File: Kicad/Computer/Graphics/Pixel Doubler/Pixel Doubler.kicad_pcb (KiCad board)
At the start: 2 copper layers, 26.7 x 49.5 mm, 17 parts, among them IC1 PI3B3251QE, IC2 74LVC16373ADL,118, IC3 74LVC2G08DP-Q100H, IC4 74LVC2G04GW-Q100H, IC5 PI3B3251QE, IC6 74LVC163PW,118, IC7 AP7365-33WG-7, J1 Conn_02x16_Counter_Clockwise

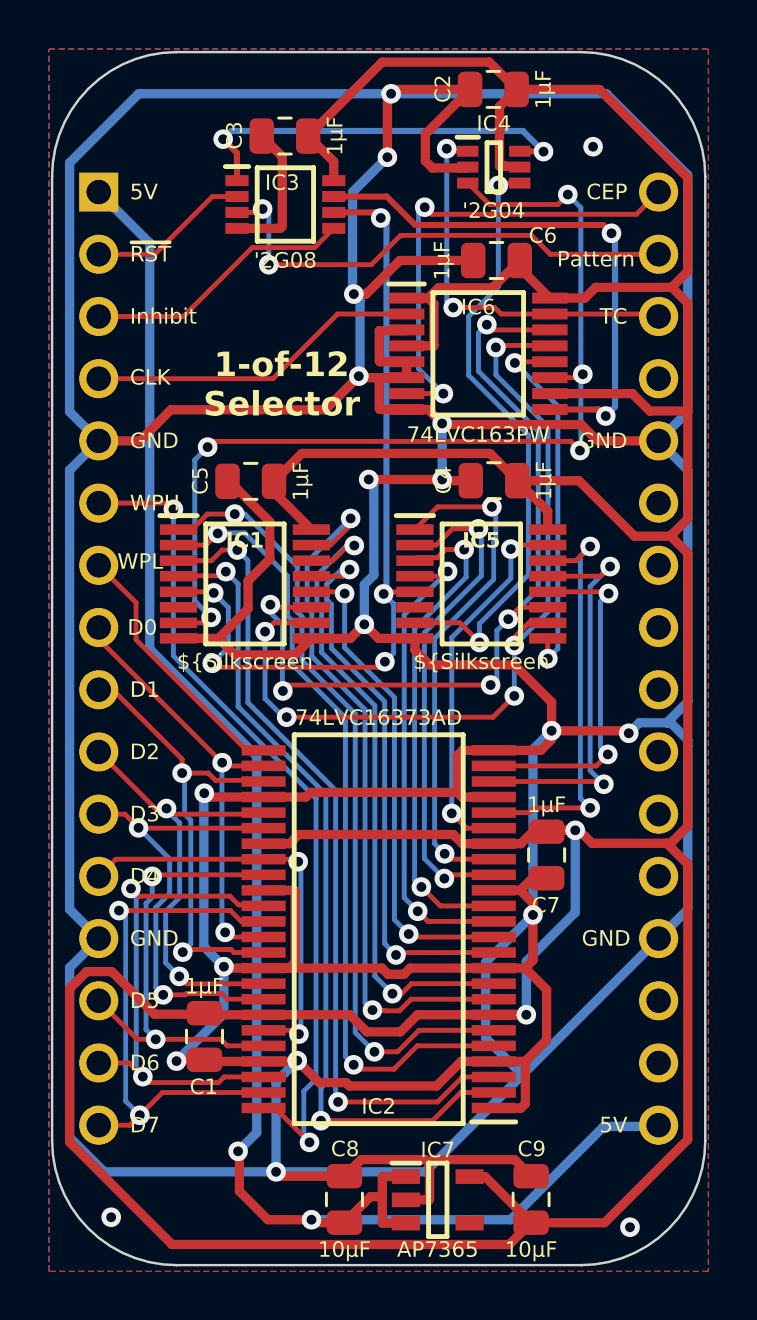
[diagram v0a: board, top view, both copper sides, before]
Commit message: Standardising DIP board layouts.
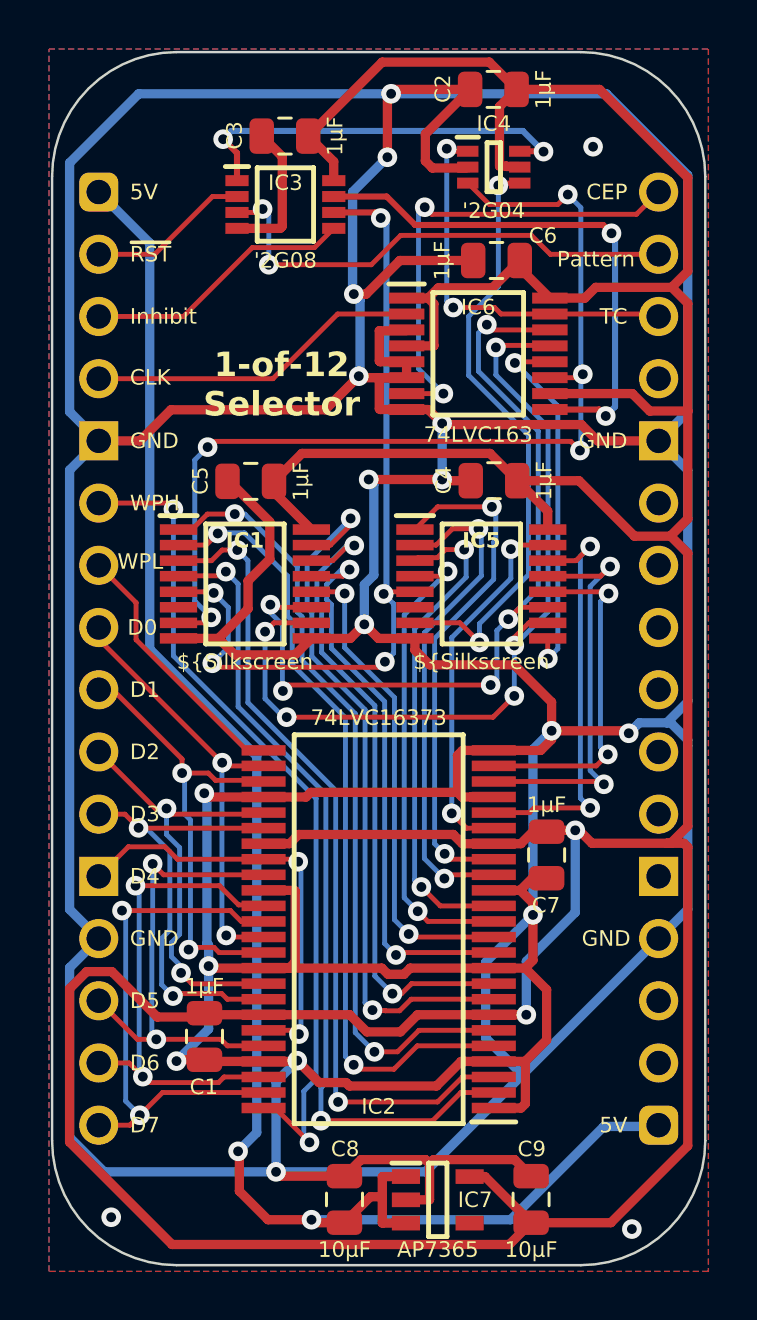
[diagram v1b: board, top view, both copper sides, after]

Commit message: Fixed and labeled the Pixel Pixel Doubler (1-of-12 selector).
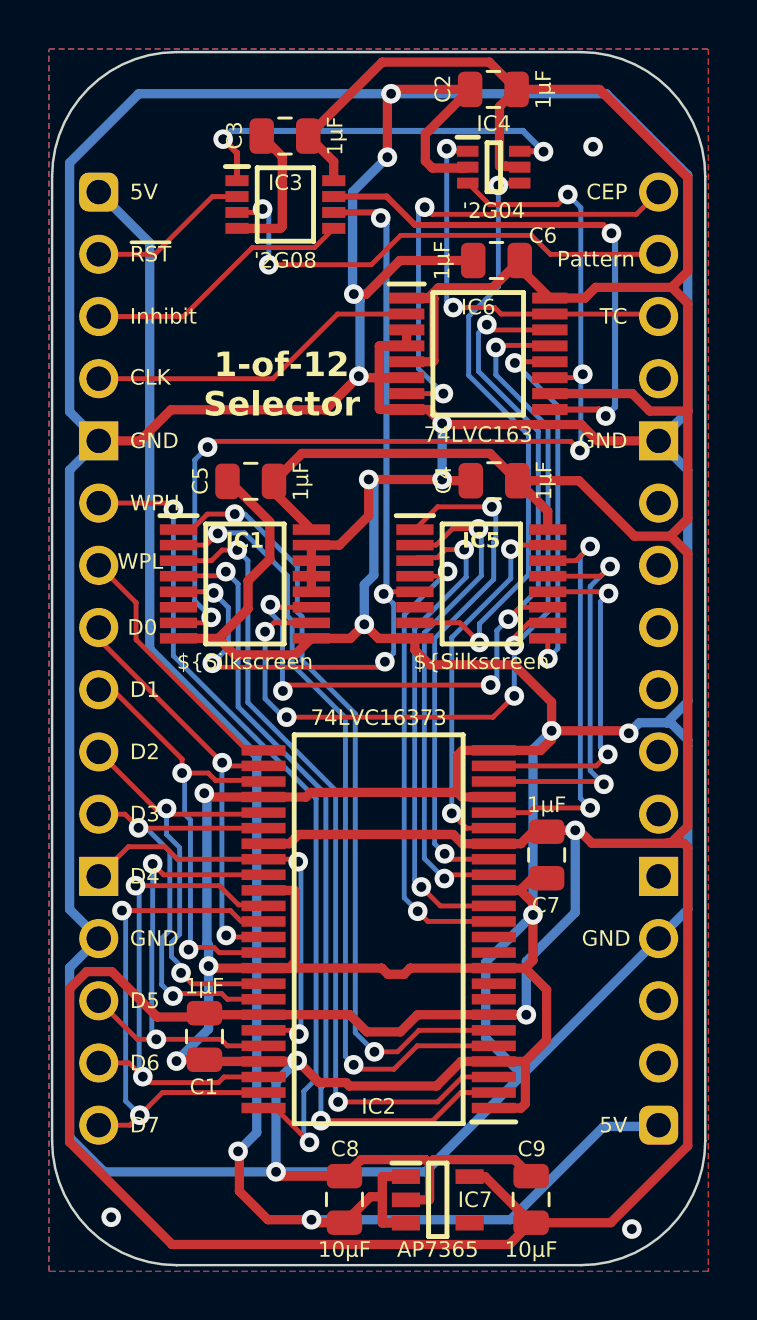
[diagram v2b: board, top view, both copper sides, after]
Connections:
- IC1 pad 1: /RPS11 -> /RPS8
- IC1 pad 12: /RPS15 -> /GND
- IC1 pad 13: /RPS14 -> /GND
- IC1 pad 14: /RPS13 -> /GND
- IC1 pad 15: /RPS12 -> /GND
- IC1 pad 2: /RPS10 -> /RPS9
- IC1 pad 3: /RPS9 -> /RPS10
- IC1 pad 4: /RPS8 -> /RPS11
- IC2 pad 11: /RPS14 -> unconnected-(IC2-1Q6-Pad11)
- IC2 pad 12: /RPS15 -> unconnected-(IC2-1Q7-Pad12)
- IC2 pad 13: /RPS0 -> /RPS7
- IC2 pad 14: /RPS1 -> /RPS6
- IC2 pad 16: /RPS2 -> /RPS5
- IC2 pad 17: /RPS3 -> /RPS4
- IC2 pad 19: /RPS4 -> /RPS3
- IC2 pad 2: /RPS8 -> /RPS11
- IC2 pad 20: /RPS5 -> /RPS2
- IC2 pad 22: /RPS6 -> /RPS1
- IC2 pad 23: /RPS7 -> /RPS0
- IC2 pad 25: /Write Pattern Low -> /Write Pattern High
- IC2 pad 26: /D0 -> /D7
- IC2 pad 27: /D1 -> /D6
- IC2 pad 29: /D2 -> /D5
- IC2 pad 3: /RPS9 -> /RPS10
- IC2 pad 30: /D3 -> /D4
- IC2 pad 32: /D4 -> /D3
- IC2 pad 33: /D5 -> /D2
- IC2 pad 35: /D6 -> /D1
- IC2 pad 36: /D7 -> /D0
- IC2 pad 37: /D0 -> /D7
- IC2 pad 38: /D1 -> /D6
- IC2 pad 40: /D2 -> /D5
- IC2 pad 41: /D3 -> /D4
- IC2 pad 43: /D4 -> /D3
- IC2 pad 44: /D5 -> /D2
- IC2 pad 46: /D6 -> /D1
- IC2 pad 47: /D7 -> /D0
- IC2 pad 48: /Write Pattern High -> /Write Pattern Low
- IC2 pad 5: /RPS10 -> /RPS9
- IC2 pad 6: /RPS11 -> /RPS8
- IC2 pad 8: /RPS12 -> unconnected-(IC2-1Q4-Pad8)
- IC2 pad 9: /RPS13 -> unconnected-(IC2-1Q5-Pad9)
- IC5 pad 1: /RPS3 -> /RPS4
- IC5 pad 12: /RPS7 -> /RPS0
- IC5 pad 13: /RPS6 -> /RPS1
- IC5 pad 14: /RPS5 -> /RPS2
- IC5 pad 15: /RPS4 -> /RPS3
- IC5 pad 2: /RPS2 -> /RPS5
- IC5 pad 3: /RPS1 -> /RPS6
- IC5 pad 4: /RPS0 -> /RPS7
- IC6 pad 4: /3.3V -> /GND
- IC6 pad 5: /GND -> /3.3V
- J1 pad 10: /D2 -> /D5
- J1 pad 11: /D3 -> /D4
- J1 pad 12: /D4 -> /D3
- J1 pad 14: /D5 -> /D2
- J1 pad 15: /D6 -> /D1
- J1 pad 16: /D7 -> /D0
- J1 pad 6: /Write Pattern High -> /Write Pattern Low
- J1 pad 7: /Write Pattern Low -> /Write Pattern High
- J1 pad 8: /D0 -> /D7
- J1 pad 9: /D1 -> /D6
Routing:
- net /RPS12: track 29.3 -> 0.00 mm, vias 2 -> 0
- net /RPS13: track 26.7 -> 0.00 mm, vias 2 -> 0
- net /Write Pattern Low: track 10.1 -> 33.7 mm, vias 0 -> 2
- net /Write Pattern High: track 33.7 -> 10.1 mm, vias 2 -> 0
- net /RPS14: track 23.2 -> 0.00 mm, vias 2 -> 0
- net /RPS15: track 19.9 -> 0.00 mm, vias 2 -> 0
- net /RPS4: track 15.3 -> 21.1 mm
- net /RPS3: track 21.1 -> 15.3 mm
- net /RPS7: track 14.2 -> 19.5 mm
- net /RPS0: track 19.5 -> 14.2 mm
- net /GND: track 351.7 -> 356.9 mm
- net /D7: track 21.9 -> 17.6 mm
- net /D0: track 17.6 -> 21.9 mm
- net /RPS5: track 17.0 -> 20.6 mm
- net /RPS2: track 20.6 -> 17.0 mm
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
